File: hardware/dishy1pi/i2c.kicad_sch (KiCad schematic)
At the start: 17 parts, among them J5 TerminalBlock_4x2.54mm, J8 TerminalBlock_4x2.54mm, U13 ISO1540DR, U14 LM75BIMX-5/NOPB, U2 LTC4311ISC6-TRPBF, U3 ISO1540DR, U4 LM75BIMX-5/NOPB

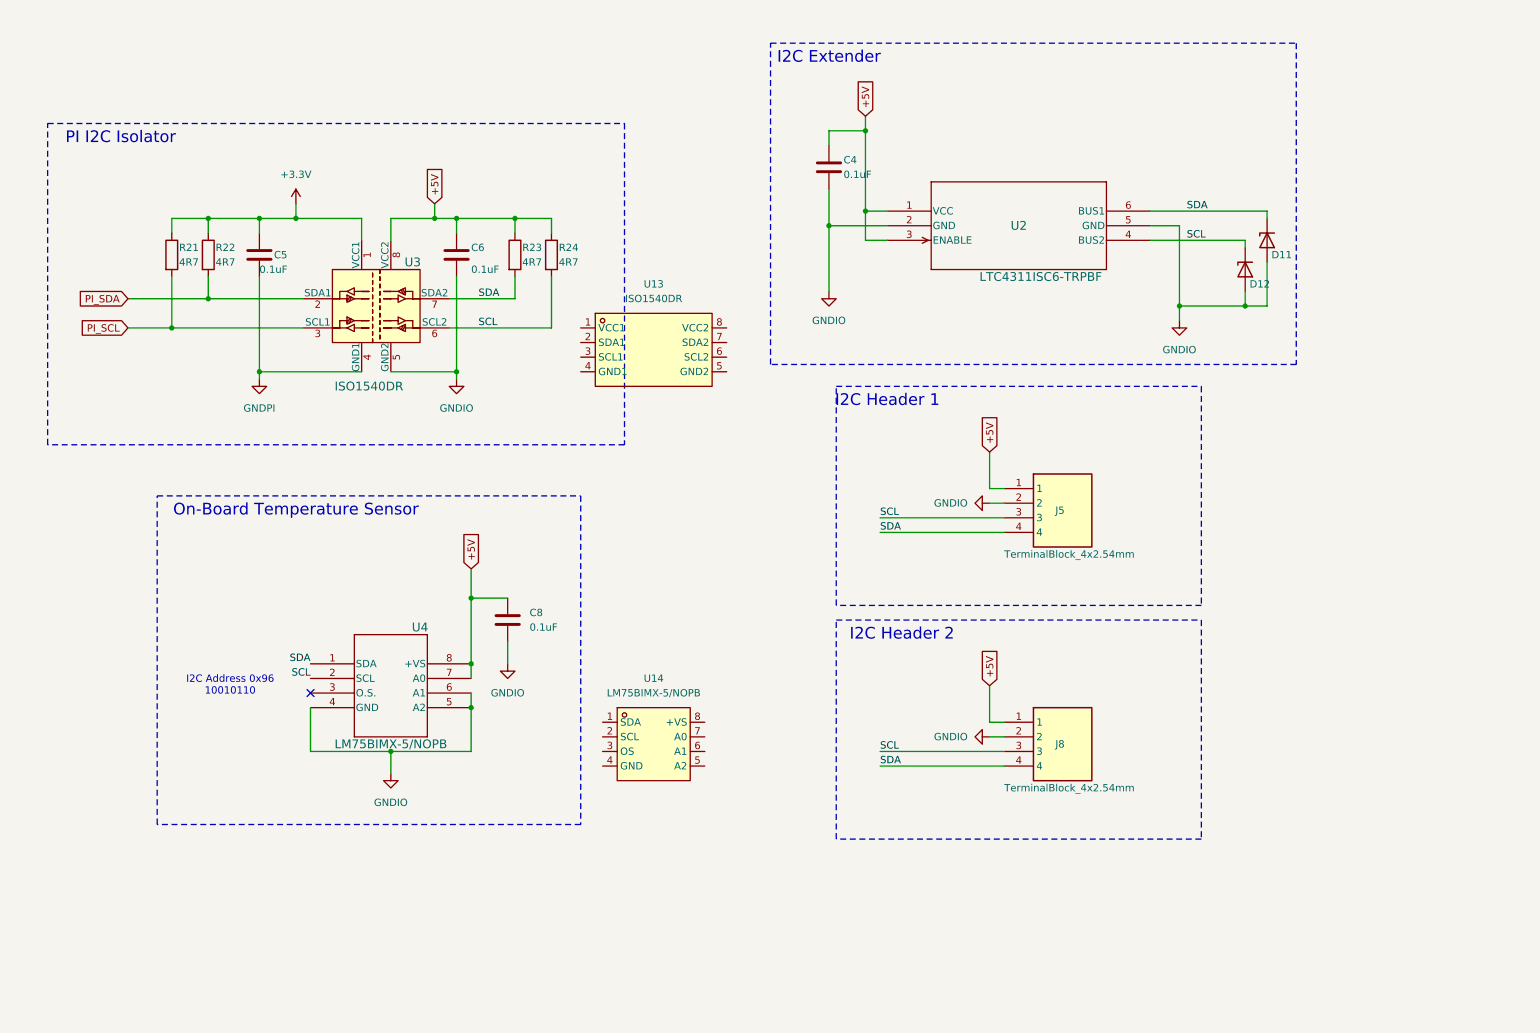
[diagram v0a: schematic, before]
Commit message: Parts place in PCB layout
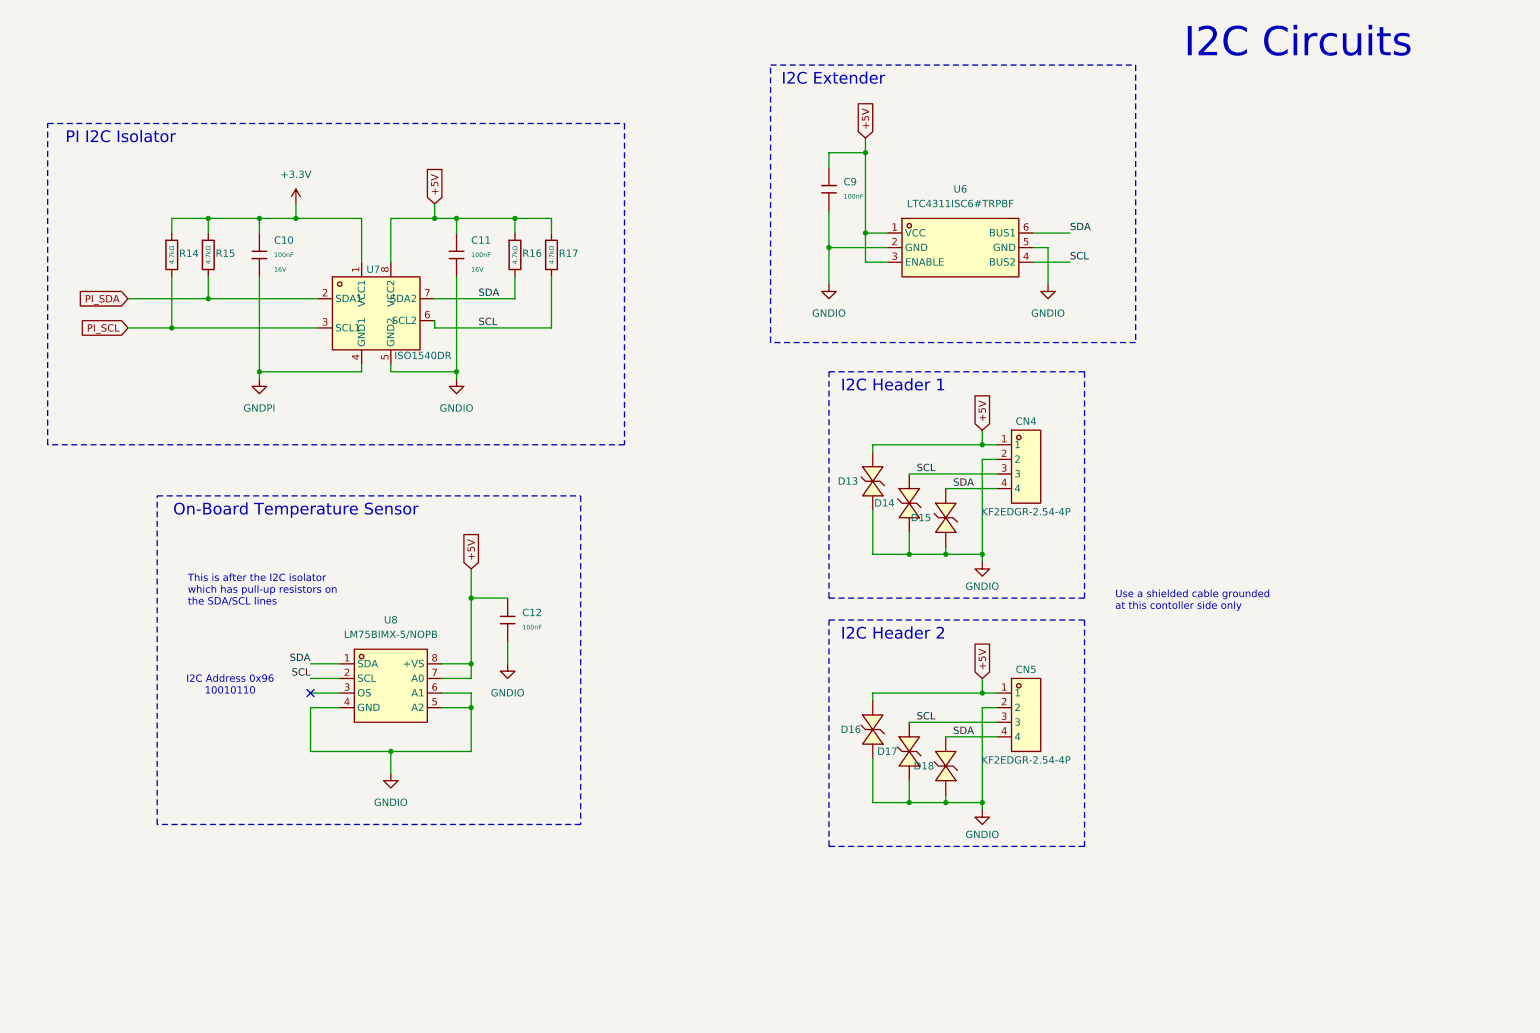
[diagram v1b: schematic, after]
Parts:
- removed C4, C5, C6, C8: 0.1uF, Capacitor_SMD:C_0402_1005Metric, symbol Device:C
- removed D11, D12: TPESD0402G05V, Diode_SMD:D_0402_1005Metric, symbol Diode:PESD5V0L1UL
- removed J5, J8: TerminalBlock_4x2.54mm, DishFootprints:TerminalBlock_4x2.54mm, symbol DishSympols:TerminalBlock_4x2.54mm
- removed R21, R22, R23, R24: 4R7, Resistor_SMD:R_0402_1005Metric, symbol Device:R
- removed U2: LTC4311ISC6-TRPBF, DishFootprints:LTC4311, symbol DishSympols:LTC4311ISC6-TRPBF
- removed U3: ISO1540DR, digikey-footprints:SOIC-8_W3.9mm, symbol dk_Digital-Isolators:ISO1540DR
- removed U4: LM75BIMX-5/NOPB, DishFootprints:M08A, symbol DishSympols:LM75BIM-3
- added C10, C11, C12, C9: 100nF, PCM_JLCPCB:C_0402, symbol PCM_JLCPCB-Capacitors:0402,100nF
- added CN4, CN5: KF2EDGR-2.54-4P, MyParts:CONN-TH_4P-P2.54_KF2EDGR-2.54-4P, symbol MyParts:KF2EDGR-2.54-4P
- added D13, D14, D15, D16, D17, D18: TPESD0402G05V, MyParts:D0402-BI, symbol MyParts:TPESD0402G05V
- added R14, R15, R16, R17: 4.7kΩ, PCM_JLCPCB:R_0402, symbol PCM_JLCPCB-Resistors:0402,4.7kΩ
- added U6: LTC4311ISC6#TRPBF, MyParts:SC-70-6_L2.2-W1.3-P0.65-LS2.2-BL, symbol MyParts:LTC4311ISC6#TRPBF
- renumbered U13 to U7, U14 to U8
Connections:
- net +3.3V: now also U7.1 (VCC1), C10.1, R14.1, R15.1
- net +5V: now also U7.8 (VCC2), U8.7 (A0), U8.8 (+VS), C11.1, C12.1, C9.1, CN4.1, CN5.1, D13.1 (K), D16.2 (A), R16.1, R17.1, U6.1 (VCC), U6.3 (ENABLE)
- net GNDIO: now also U7.5 (GND2), U8.4 (GND), U8.5 (A2), U8.6 (A1), C11.2, C12.2, C9.2, CN4.2, CN5.2, D13.2 (A), D14.2 (A), D15.2 (A), D16.1 (K), D17.1 (K), D18.1 (K), U6.2 (GND), U6.5 (GND)
- net GNDPI: now also U7.4 (GND1), C10.2
- net PI_SCL: now also U7.3 (SCL1), R14.2
- net PI_SDA: now also U7.2 (SDA1), R15.2
- net SCL: now also U7.6 (SCL2), U8.2 (SCL), CN4.3, CN5.3, D14.1 (K), D17.2 (A), R17.2, U6.4 (BUS2)
- net SDA: now also U7.7 (SDA2), U8.1 (SDA), CN4.4, CN5.4, D15.1 (K), D18.2 (A), R16.2, U6.6 (BUS1)
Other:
- note added: "I2C Circuits"
- note added: "This is after the I2C isolator which has pull-up resistors on the SDA/SCL lines"
- note added: "Use a shielded cable grounded at this contoller side only"
- moved on the sheet: U7, U8

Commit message: Ground and Power planes placed
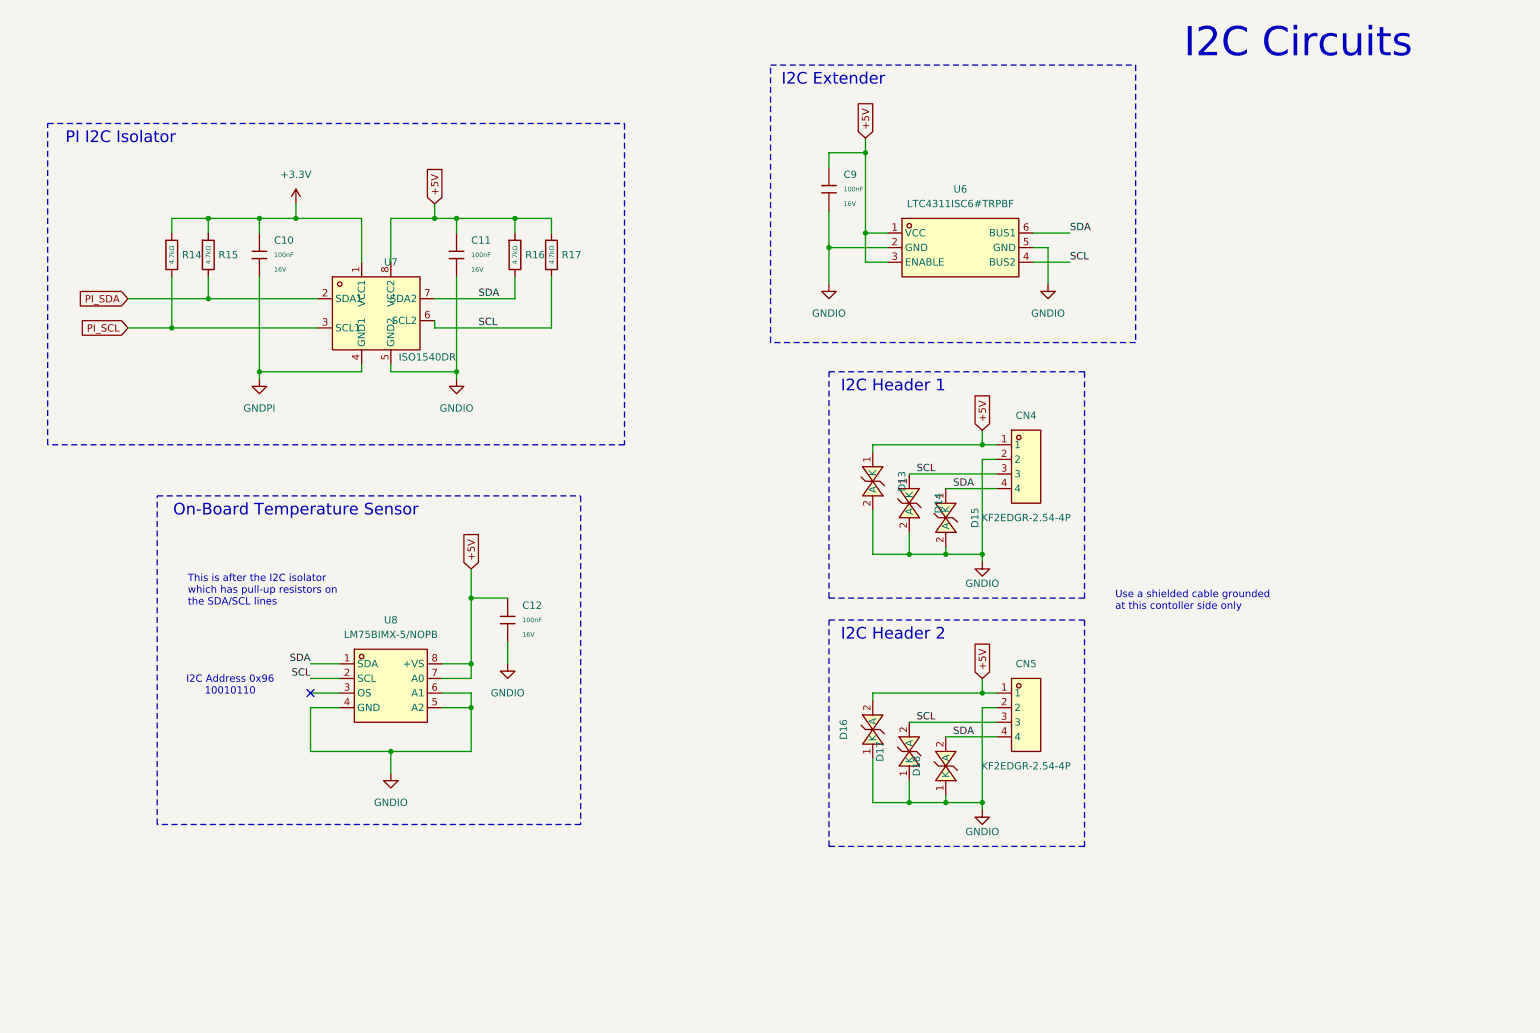
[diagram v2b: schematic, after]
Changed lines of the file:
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@@
 		(dnp no)
 		(property "Reference" "CN4"
-			(at 204.47 88.646 0)
+			(at 204.47 87.63 0)
 			(effects
 				(font
@@
 		)
 		(property "Value" "KF2EDGR-2.54-4P"
-			(at 204.47 104.394 0)
+			(at 204.47 105.41 0)
 			(effects
 				(font
@@
 		(fields_autoplaced yes)
 		(property "Reference" "C12"
-			(at 116.84 121.9199 0)
+			(at 116.84 120.6499 0)
 			(effects
 				(font
@@
 		)
 		(property "Value" "100nF"
-			(at 116.84 124.46 0)
+			(at 116.84 123.19 0)
 			(effects
 				(font
@@
 				)
 				(justify left)
-				(hide yes)
 			)
 		)
@@
 		(dnp no)
 		(property "Reference" "R15"
-			(at 63.5 59.436 0)
+			(at 64.008 59.69 0)
 			(effects
 				(font
@@
 		(dnp no)
 		(property "Reference" "CN5"
-			(at 204.47 131.826 0)
+			(at 204.47 130.81 0)
 			(effects
 				(font
@@
 		)
 		(property "Value" "KF2EDGR-2.54-4P"
-			(at 204.47 147.574 0)
+			(at 204.47 148.59 0)
 			(effects
 				(font
@@
 		(fields_autoplaced yes)
 		(property "Reference" "C9"
-			(at 172.72 46.9899 0)
+			(at 172.72 45.7199 0)
 			(effects
 				(font
@@
 		)
 		(property "Value" "100nF"
-			(at 172.72 49.53 0)
+			(at 172.72 48.26 0)
 			(effects
 				(font
@@
 				)
 				(justify left)
-				(hide yes)
 			)
 		)
@@
 		(dnp no)
 		(property "Reference" "R14"
-			(at 57.15 59.436 0)
+			(at 57.658 59.69 0)
 			(effects
 				(font
@@
 		)
 		(property "Value" "GNDIO"
-			(at 196.85 117.348 0)
+			(at 196.85 116.84 0)
 			(effects
 				(font
@@
 		(dnp no)
 		(property "Reference" "U7"
-			(at 90.932 62.23 0)
+			(at 93.98 60.96 0)
 			(effects
 				(font
@@
 		)
 		(property "Value" "ISO1540DR"
-			(at 99.568 77.216 0)
+			(at 100.33 77.47 0)
 			(effects
 				(font
@@
 		(dnp no)
 		(property "Reference" "R17"
-			(at 123.19 59.436 0)
+			(at 123.698 59.69 0)
 			(effects
 				(font
@@
 		(dnp no)
 		(property "Reference" "D17"
-			(at 182.118 146.05 90)
-			(effects
-				(font
-					(size 1.27 1.27)
-				)
-				(justify left)
+			(at 179.07 146.05 0)
+			(effects
+				(font
+					(size 1.27 1.27)
+				)
 			)
 		)
@@
 		(dnp no)
 		(property "Reference" "D14"
-			(at 178.054 102.87 90)
-			(effects
-				(font
-					(size 1.27 1.27)
-				)
-				(justify left)
+			(at 189.23 102.87 0)
+			(effects
+				(font
+					(size 1.27 1.27)
+				)
 			)
 		)
@@
 		(dnp no)
 		(property "Reference" "D15"
-			(at 184.404 105.41 90)
-			(effects
-				(font
-					(size 1.27 1.27)
-				)
-				(justify left)
+			(at 195.58 105.41 0)
+			(effects
+				(font
+					(size 1.27 1.27)
+				)
 			)
 		)
@@
 		(dnp no)
 		(property "Reference" "R16"
-			(at 116.84 59.436 0)
+			(at 117.348 59.69 0)
 			(effects
 				(font
@@
 		(dnp no)
 		(property "Reference" "D13"
-			(at 171.704 99.06 90)
-			(effects
-				(font
-					(size 1.27 1.27)
-				)
-				(justify left)
+			(at 182.88 99.06 0)
+			(effects
+				(font
+					(size 1.27 1.27)
+				)
 			)
 		)
@@
 		(dnp no)
 		(property "Reference" "D18"
-			(at 188.468 148.59 90)
-			(effects
-				(font
-					(size 1.27 1.27)
-				)
-				(justify left)
+			(at 185.42 148.59 0)
+			(effects
+				(font
+					(size 1.27 1.27)
+				)
 			)
 		)
@@
 		(dnp no)
 		(property "Reference" "D16"
-			(at 175.768 142.24 90)
-			(effects
-				(font
-					(size 1.27 1.27)
-				)
-				(justify left)
+			(at 172.72 142.24 0)
+			(effects
+				(font
+					(size 1.27 1.27)
+				)
 			)
 		)
@@
 		)
 		(property "Value" "GNDIO"
-			(at 196.85 160.528 0)
-			(effects
-				(font
+			(at 196.85 160.02 0)
+			(effects
+				(font
